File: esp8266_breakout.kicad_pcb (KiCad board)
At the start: 2 copper layers, 43 parts, among them CON1 USB-MICRO-B2, P1 CONN_12, Q1 MOS_P, Q2 MOS_N, SW1 SW_PUSH, U1 NCP1117LP, U2 ESP8266-3, U3 FT230XS

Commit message: Starting reworking for ordering pcbs
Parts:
- removed G***: logo_hacker_cutop_10_0mm, logo_hacker_cutop_10_0mm
- moved R12 169.8 mm to (91.4, 80.0)
- moved R13 169.8 mm to (91.4, 85.1)
- moved R14 169.8 mm to (91.4, 82.5)
- moved R15 169.8 mm to (91.4, 77.5)
- moved R16 169.8 mm to (91.4, 74.9)
- moved R17 169.8 mm to (91.4, 72.4)
- moved R5 169.8 mm to (91.4, 69.8)
- moved SW1 165.9 mm to (86.4, 62.2)
- moved P1 165.2 mm to (95.9, 76.2)
- moved 1PIN 160.7 mm to (102.2, 99.1)
- moved 1PIN 160.7 mm to (59.7, 99.1)
- moved C1 160.7 mm to (64.8, 87.1)
- moved C10 160.7 mm to (60.7, 65.0)
- moved C4 160.7 mm to (71.8, 91.4)
- moved C5 160.7 mm to (74.3, 89.5)
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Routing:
- net /PROG_SW: track 52.4 -> 12.8 mm, vias 2 -> 0
- net +3.3V: track 107.2 -> 77.8 mm, vias 2 -> 1
- net VCC: track 104.3 -> 81.6 mm, vias 3 -> 2
- net /GPIO0: track 49.4 -> 36.3 mm, vias 2 -> 1
- net N-0000016: track 36.3 -> 24.5 mm
- net N-0000014: track 43.6 -> 36.4 mm, vias 2 -> 1
- net N-000006: track 6.63 -> 0.00 mm
- net N-0000010: track 42.7 -> 36.6 mm, vias 2 -> 1
- net N-0000026: track 43.1 -> 37.5 mm, vias 2 -> 1
- net N-0000015: track 50.9 -> 45.3 mm, vias 2 -> 1
- net N-0000021: track 5.22 -> 0.00 mm
- net N-0000013: track 38.6 -> 34.2 mm, vias 2 -> 1
- net N-000005: track 3.56 -> 0.00 mm
- net /CON_GPIO2: track 2.61 -> 0.00 mm
- net /CON_GPIO18: track 2.61 -> 0.00 mm
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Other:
- rule via_min_drill: 0.3 -> 0.2
- rule via_min_size: 0.7 -> 0.6

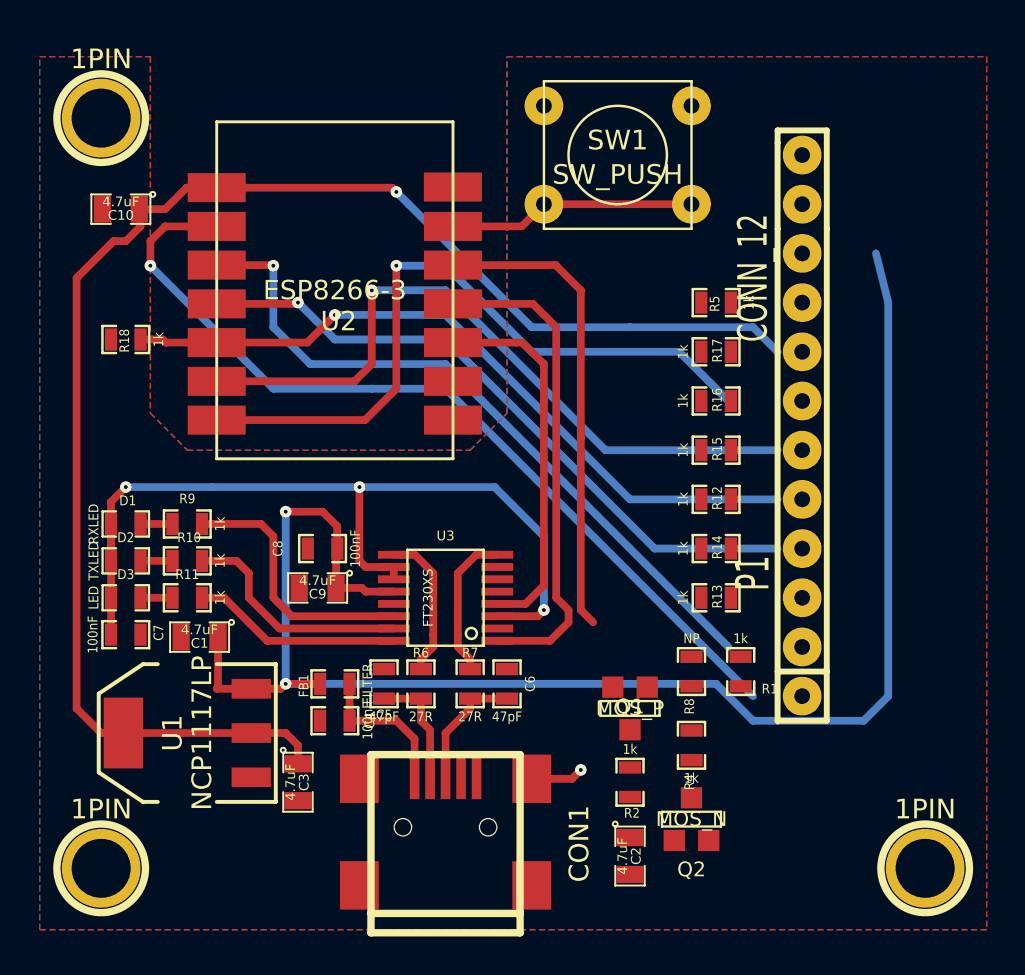
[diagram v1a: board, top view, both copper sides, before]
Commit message: Finished first reworked layout version
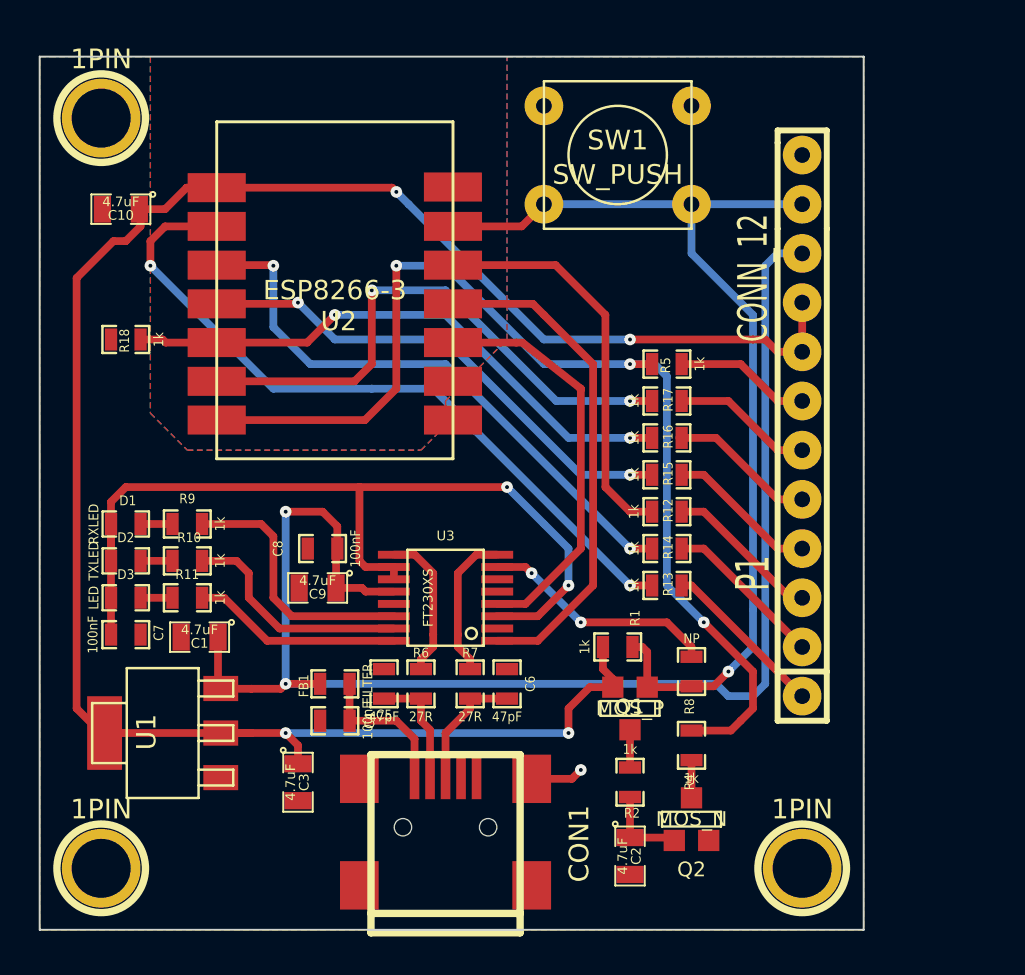
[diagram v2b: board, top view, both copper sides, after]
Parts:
- U1: footprint SOT223 -> sot223
- moved R1 6.48 mm to (86.4, 87.6), turned to 0 degrees
- moved 1PIN 6.35 mm to (95.9, 99.1)
- moved R5 4.07 mm to (88.9, 73.0)
- moved R17 3.59 mm to (88.9, 74.9)
- moved R16 3.17 mm to (88.9, 76.8)
- moved R15 2.84 mm to (88.9, 78.7)
- moved R13 2.62 mm to (88.9, 84.5)
- moved R12 2.62 mm to (88.9, 80.6)
- moved R14 2.54 mm to (88.9, 82.5)
- moved U1 1.27 mm to (62.9, 92.1)
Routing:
- net /PROG_SW: track 12.8 -> 51.7 mm, vias 0 -> 2
- net +3.3V: track 77.8 -> 103.9 mm, vias 1 -> 4
- net /GPIO0: track 36.3 -> 56.4 mm, vias 1 -> 3
- net N-0000021: track 0.00 -> 12.3 mm, vias 0 -> 2
- net /CON_GPIO14: track 0.00 -> 8.59 mm
- net /CON_GPIO12: track 0.00 -> 8.33 mm
- net /CON_GPIO18: track 0.00 -> 8.06 mm
- net N-0000013: track 34.2 -> 26.2 mm, vias 1 -> 2
- net /CON_GPIO13: track 0.00 -> 7.80 mm
- net N-0000026: track 37.5 -> 29.7 mm, vias 1 -> 2
- net /CON_GPIO15: track 0.00 -> 7.67 mm
- net N-0000015: track 45.3 -> 37.8 mm, vias 1 -> 2
- net N-0000010: track 36.6 -> 29.0 mm, vias 1 -> 2
- net /CON_GPIO2: track 0.00 -> 7.28 mm
- net /CON_GPIO0: track 0.00 -> 7.01 mm
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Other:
- board outline added: 42.5 x 45.1 mm

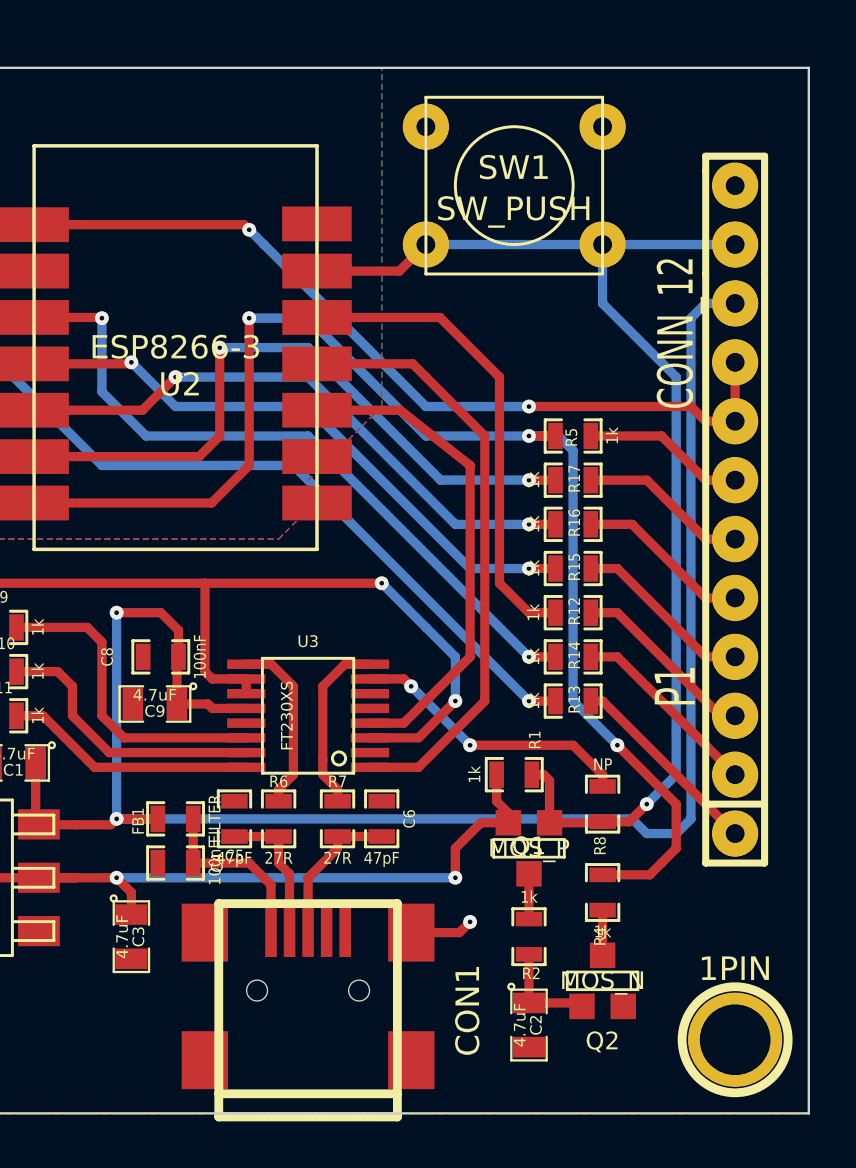
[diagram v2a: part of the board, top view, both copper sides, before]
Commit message: Added ufl connector cleaned up schematic
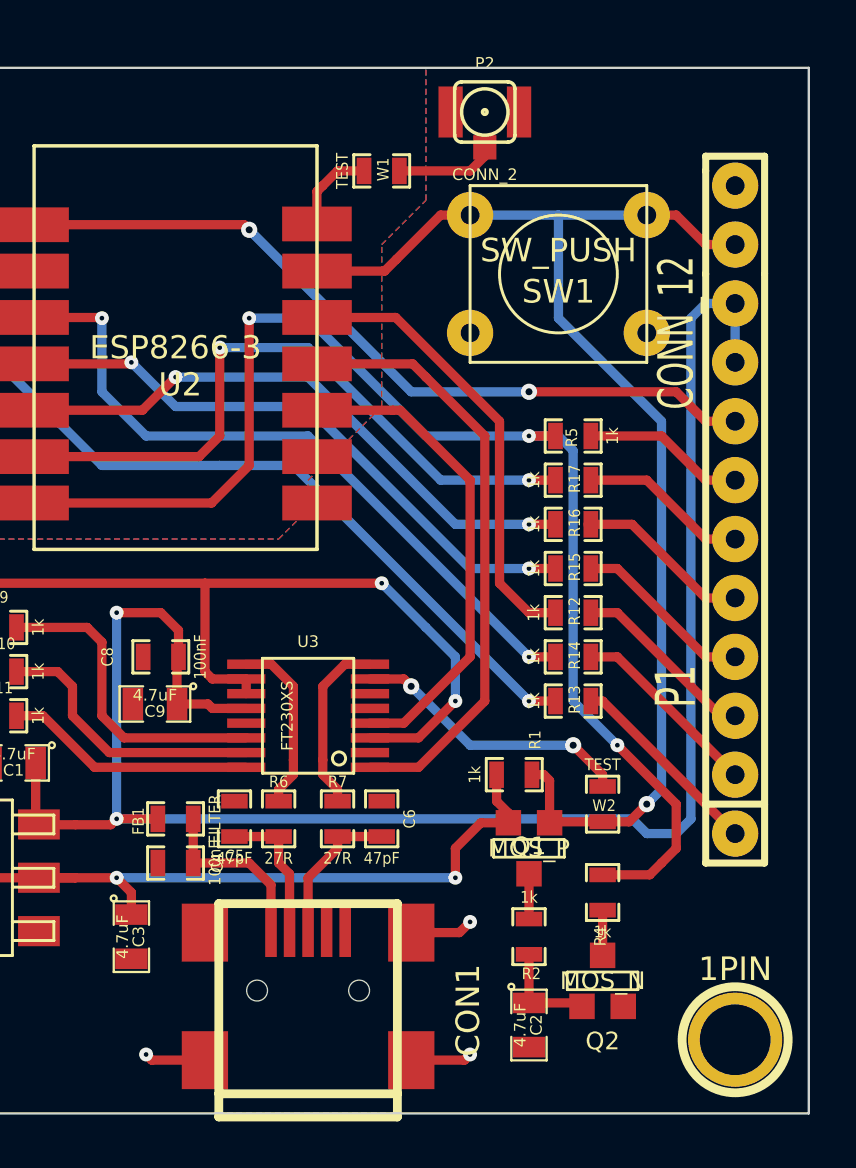
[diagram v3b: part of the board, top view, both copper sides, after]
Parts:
- removed R8: NP, SM0603_Resistor
- added P2: CONN_2, coaxial_u.fl-r-smt-1, F.Cu at (85.1, 59.1)
- added W1: TEST, SM0603_Resistor, F.Cu at (80.6, 61.6)
- added W2: TEST, SM0603_Resistor, F.Cu at (90.2, 88.9)
- moved SW1 4.26 mm to (88.3, 66.0), turned to 180 degrees
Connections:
- net /CON_GPIO0 renamed CON_GPIO0
- net /CON_GPIO12 renamed CON_GPIO12
- net /CON_GPIO13 renamed CON_GPIO13
- net /CON_GPIO14 renamed CON_GPIO14
- net /CON_GPIO15 renamed CON_GPIO15
- net /CON_GPIO18 renamed CON_GPIO18
- net /CON_GPIO2 renamed CON_GPIO2
- net /FT230_RX renamed FT230_RX
- net /FT230_TX renamed FT230_TX
- net /GPIO0 renamed GPIO0
- net /PROG_SW renamed PROG_SW
- P1 pad 9: +3.3V -> VCC
- U2 pad 7: (no net) -> N-0000024
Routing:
- net GND: track 2.73 -> 8.00 mm, vias 1 -> 3
- net N-0000030: track 0.00 -> 4.33 mm
- net N-0000024: track 0.00 -> 3.80 mm
- net PROG_SW: track 51.7 -> 54.3 mm, vias 2 -> 1
- net +3.3V: track 103.9 -> 101.4 mm
- net VCC: track 75.3 -> 77.9 mm
- net N-0000034: track 20.8 -> 19.6 mm

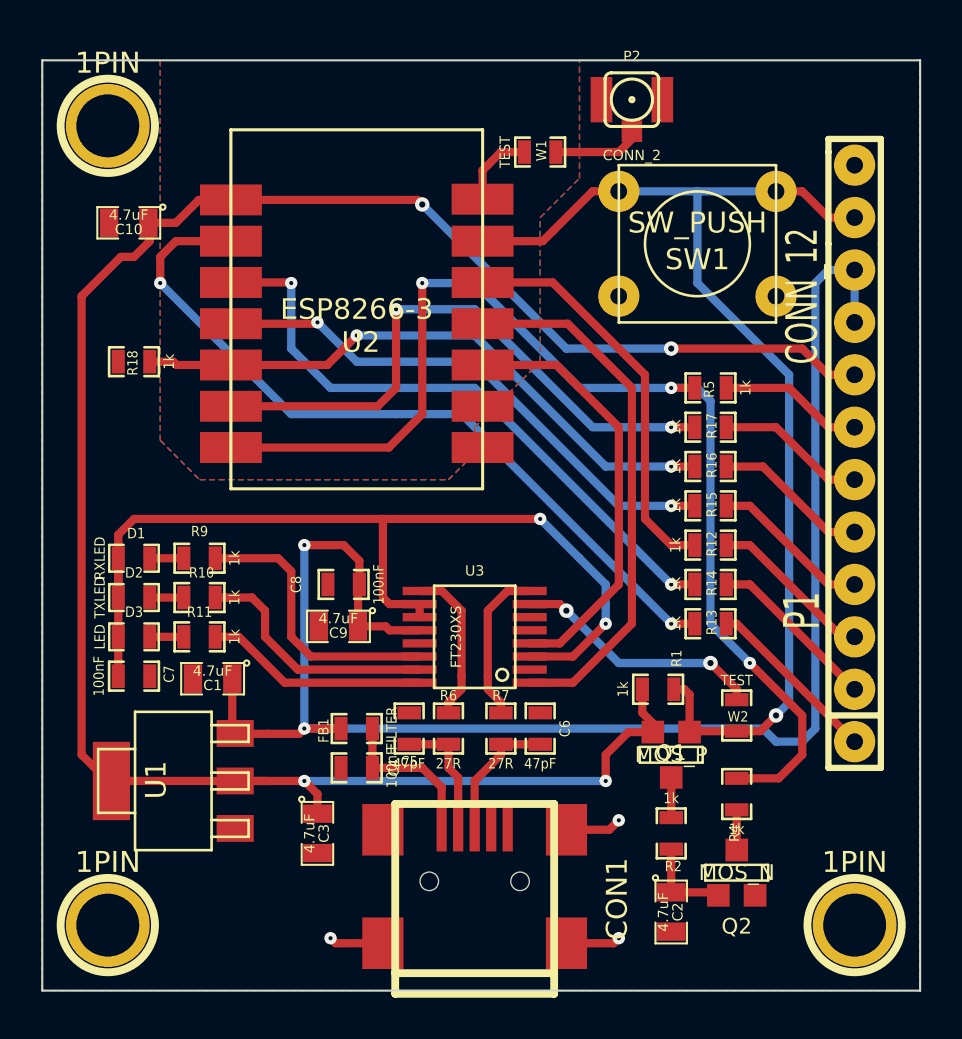
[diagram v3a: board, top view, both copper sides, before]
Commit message: Added logos and fancy silkscreen
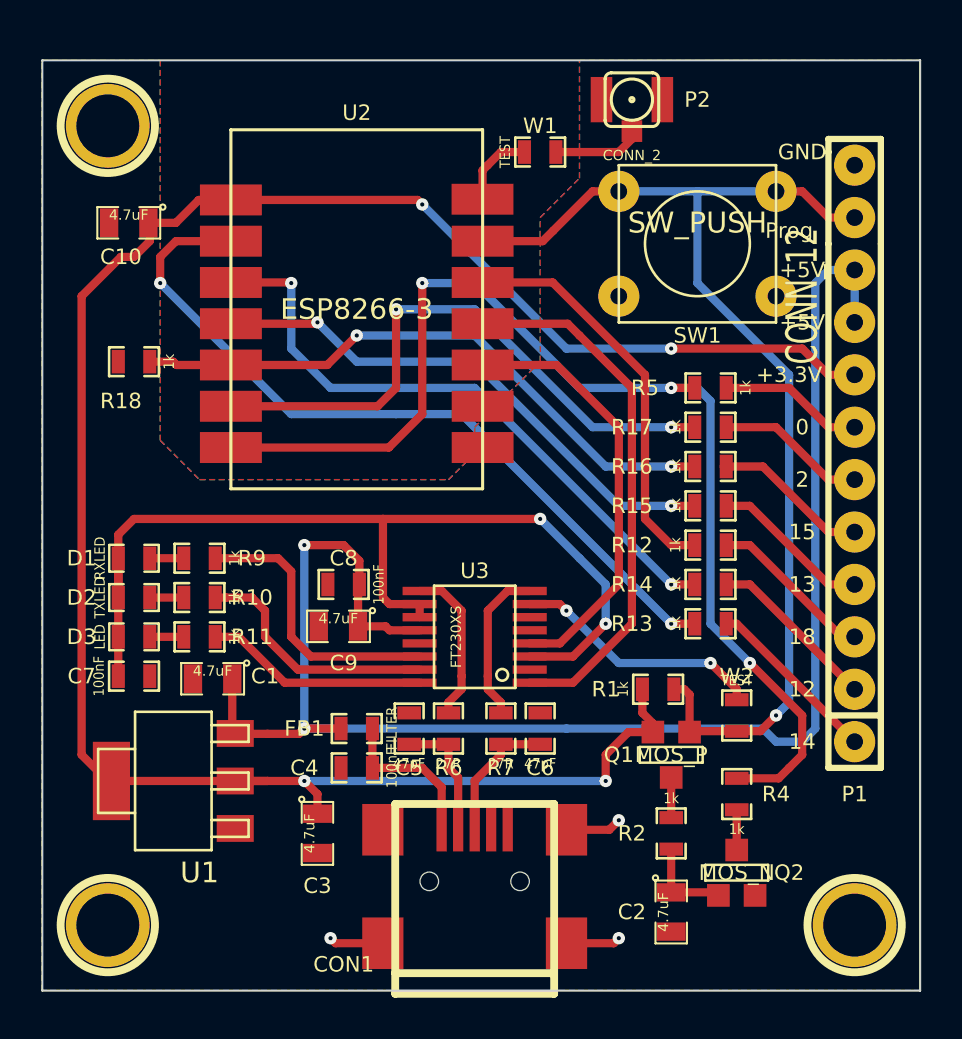
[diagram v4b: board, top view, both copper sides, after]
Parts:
- added G***: chaosinkl_silkbot_25_00mm, chaosinkl_silkbot_25_00mm, B.Cu at (71.1, 87.6)
- added G***: logo_hacker_silkbot_15_00mm, logo_hacker_silkbot_15_00mm, B.Cu at (71.8, 66.7)
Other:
- board text added: "+3.3V"
- board text added: "+5V"
- board text added: "0"
- board text added: "12"
- board text added: "13"
- board text added: "14"
- board text added: "15"
- board text added: "18"
- board text added: "2"
- board text added: "ESP8266 Breakout"
- board text added: "GND"
- board text added: "Original design by limpkin.fr"
- board text added: "Prog"

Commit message: Added version and github url
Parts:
- moved G*** 2.84 mm to (72.4, 90.2)
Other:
- board text added: "V.1.0"
- board text added: "https://github.com/LongHairedHacker/ESP8266-breakout"
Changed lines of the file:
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@@
     (area 46.610002 52.395001 99.110001 104.864933)
     (thickness 1.6)
-    (drawings 20)
+    (drawings 22)
     (tracks 293)
     (zones 0)
@@
     (visible_elements 7FFF7FFD)
     (pcbplotparams
-      (layerselection 32769)
+      (layerselection 3178497)
       (usegerberextensions false)
       (excludeedgelayer true)
       (linewidth 0.150000)
       (plotframeref false)
-      (viasonmask false)
+      (viasonmask true)
       (mode 1)
       (useauxorigin false)
@@
       (padsonsilk false)
       (subtractmaskfromsilk false)
-      (outputformat 5)
+      (outputformat 2)
       (mirror false)
       (drillshape 2)
@@
   )
   (module chaosinkl_silkbot_25_00mm (layer Dessous.Cu)
-    (at 71.12 87.63)
+    (at 72.39 90.17)
     (fp_text reference G*** (at 0 -9.3091) (layer B.SilkS) hide
       (effects (font (size 0.49784 0.49784) (thickness 0.09906)) (justify mirror))
@@
       (xy -0.21336 -4.14274) (xy -0.2159 -4.13004) (xy -0.2159 -4.10972) (xy -0.2159 -4.10972)) (layer B.SilkS) (width 0.00254))
   )
+  (gr_text V.1.0 (at 62.23 77.47) (layer B.SilkS)
+    (effects (font (size 0.9 0.9) (thickness 0.225)) (justify mirror))
+  )
+  (gr_text https://github.com/LongHairedHacker/ESP8266-breakout (at 77.47 80.01) (layer B.SilkS)
+    (effects (font (size 0.75 0.75) (thickness 0.1875)) (justify mirror))
+  )
   (gr_text "Original design by limpkin.fr" (at 77.47 100.965) (layer B.SilkS)
     (effects (font (size 0.75 0.75) (thickness 0.1875)) (justify mirror))
   )
-  (gr_text "ESP8266 Breakout" (at 73.66 76.835) (layer B.SilkS)
+  (gr_text "ESP8266 Breakout" (at 80.01 76.835) (layer B.SilkS)
     (effects (font (size 2 2) (thickness 0.5)) (justify mirror))
   )
